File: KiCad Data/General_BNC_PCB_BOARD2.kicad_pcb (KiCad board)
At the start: 2 copper layers, 132.1 x 55.9 mm, 16 parts, among them P1 Potentiometer, Digikey P/N: 3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

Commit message: Add files via upload
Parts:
- added TP2: TestPoint, GENERAL PROJECT - NUMBER 1 LIBRARY - FOOTPRINTS:TestPoint, F.Cu at (71.1, 81.3)
- moved DP4T1 53.1 mm to (97.7, 101.6)
- moved SWT1 23.7 mm to (54.9, 106.5), turned to 90 degrees
- moved R1 23.4 mm to (66.0, 104.1)
- moved LED2 22.7 mm to (145.6, 103.6)
- moved LED3 22.7 mm to (151.1, 103.6)
- moved LED4 22.7 mm to (156.7, 103.6)
- moved LED1 22.7 mm to (140.1, 103.6)
- moved TP1 17.3 mm to (64.8, 81.3)
- moved P1 12.6 mm to (63.6, 83.2)
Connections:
- IDC1 pad 1: GND -> Net-(BNC1-Ext)
- IDC1 pad 10: Net-(BNC2-In) -> Net-(BNC3-In)
- IDC1 pad 11: Net-(BNC3-In) -> Net-(BNC4-In)
- IDC1 pad 12: Net-(BNC4-In) -> Net-(BNC5-In)
- IDC1 pad 13: Net-(BNC5-In) -> Net-(BNC6-In)
- IDC1 pad 14: Net-(BNC6-In) -> GND
- IDC1 pad 2: Net-(BNC1-Ext) -> Net-(BNC2-Ext)
- IDC1 pad 3: Net-(BNC2-Ext) -> Net-(BNC3-Ext)
- IDC1 pad 4: Net-(BNC3-Ext) -> Net-(BNC4-Ext)
- IDC1 pad 5: Net-(BNC4-Ext) -> Net-(BNC5-Ext)
- IDC1 pad 6: Net-(BNC5-Ext) -> Net-(BNC6-Ext)
- IDC1 pad 7: Net-(BNC6-Ext) -> GND
- IDC1 pad 8: GND -> Net-(BNC1-In)
- IDC1 pad 9: Net-(BNC1-In) -> Net-(BNC2-In)
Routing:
- net Net-(LED2-A): track 52.2 -> 85.2 mm
- net Net-(LED3-A): track 29.4 -> 62.1 mm
- net Net-(LED1-A): track 12.9 -> 44.9 mm
- net Net-(LED4-A): track 37.3 -> 68.8 mm
- net Net-(DP4T1-Pad1): track 64.3 -> 33.4 mm
- net Net-(P1-Pad3): track 32.0 -> 25.8 mm
- net Net-(BNC6-In): track 92.8 -> 97.6 mm
- net Net-(BNC5-In): track 119.5 -> 123.7 mm
- net Net-(BNC4-Ext): track 24.7 -> 27.3 mm
- net Net-(BNC1-In): track 61.0 -> 58.5 mm
- net Net-(BNC5-Ext): track 41.2 -> 42.7 mm
- net Net-(SWT1-B): track 12.8 -> 11.4 mm
- net Net-(BNC2-Ext): track 36.6 -> 35.4 mm
- net Net-(SWT1-A): track 23.0 -> 21.9 mm
- net Net-(BNC3-Ext): track 23.7 -> 22.6 mm
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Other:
- board size 132.1 x 55.9 mm -> 132.1 x 45.7 mm

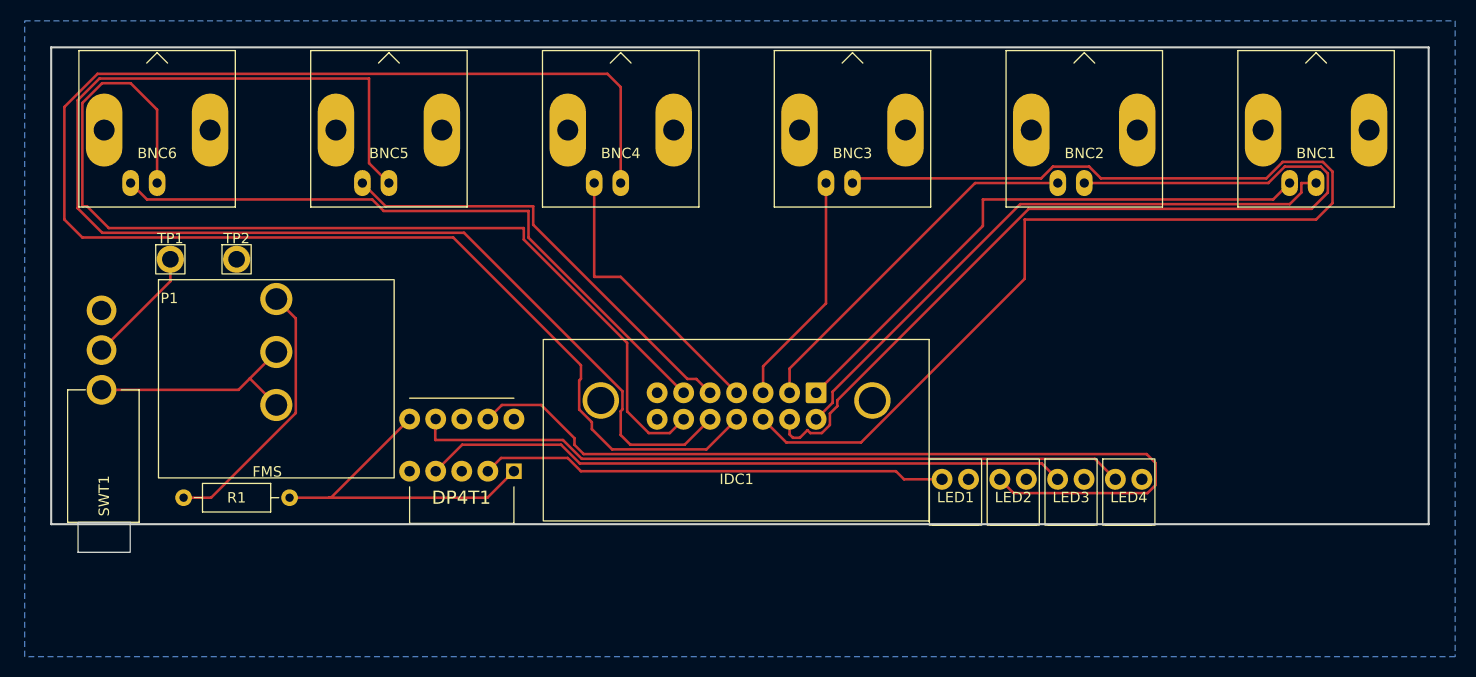
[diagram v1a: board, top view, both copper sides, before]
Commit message: Updated distance to edge of PCB for BNC's
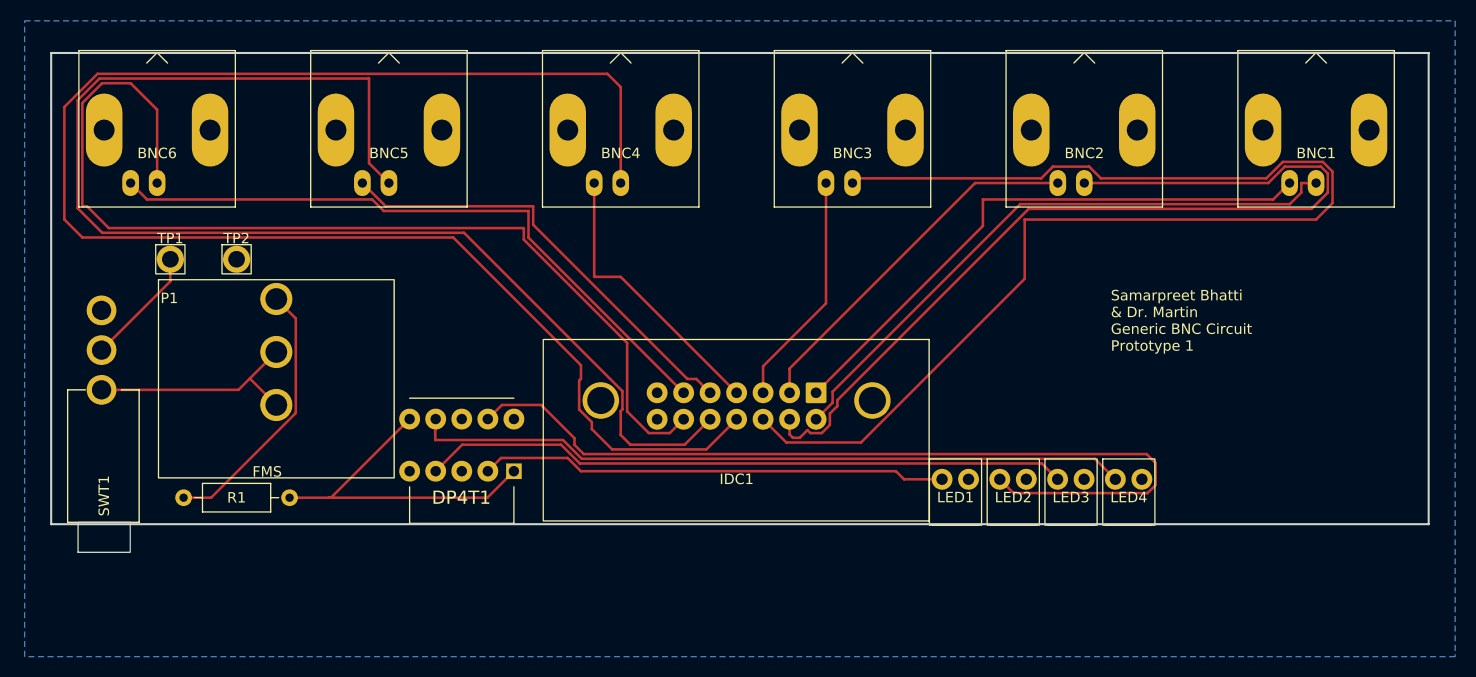
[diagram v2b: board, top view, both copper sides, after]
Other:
- board size 132.1 x 45.7 mm -> 132.1 x 45.2 mm
- board text added: "Samarpreet Bhatti & Dr. Martin Generic BNC Circuit Prototype 1"
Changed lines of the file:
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@@
     (pad "MH" thru_hole oval (at 5.08 -5.08) (size 3.5 7) (drill 2.01) (layers "*.Cu" "*.Mask"))
   )
-  (gr_rect (start 53.34 60.96) (end 185.42 106.68)
+  (gr_rect (start 53.34 61.5) (end 185.42 106.68)
     (stroke (width 0.2) (type default)) (fill none) (layer "Edge.Cuts"))
+  (gr_text "Samarpreet Bhatti\n& Dr. Martin\nGeneric BNC Circuit\nPrototype 1" (at 154.94 90.17) (layer "F.SilkS")
+    (effects (font (size 1 1) (thickness 0.15)) (justify left bottom))
+  )
   (segment (start 128.27 93.98) (end 128.27 95.0325) (width 0.25) (layer "F.Cu") (net 1))
   (segment (start 173.21 73.97) (end 173.21 74.88599) (width 0.25) (layer "F.Cu") (net 1))

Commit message: Updated board
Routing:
- net Net-(BNC6-Ext): track 62.8 -> 62.0 mm
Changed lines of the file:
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@@
   (segment (start 56.78 76.2) (end 58.87 78.29) (width 0.25) (layer "F.Cu") (net 11))
   (segment (start 84.123604 75.545) (end 62.535 75.545) (width 0.25) (layer "F.Cu") (net 12))
-  (segment (start 99.10901 79.20651) (end 99.10901 76.65) (width 0.25) (layer "F.Cu") (net 12))
-  (segment (start 99.10901 76.65) (end 85.228604 76.65) (width 0.25) (layer "F.Cu") (net 12))
-  (segment (start 85.228604 76.65) (end 84.123604 75.545) (width 0.25) (layer "F.Cu") (net 12))
+  (segment (start 99.10901 79.20651) (end 99.10901 78.103604) (width 0.25) (layer "F.Cu") (net 12))
+  (segment (start 98.845406 77.84) (end 86.418604 77.84) (width 0.25) (layer "F.Cu") (net 12))
+  (segment (start 62.535 75.545) (end 60.96 73.97) (width 0.25) (layer "F.Cu") (net 12))
+  (segment (start 86.418604 77.84) (end 84.123604 75.545) (width 0.25) (layer "F.Cu") (net 12))
+  (segment (start 99.10901 78.103604) (end 98.845406 77.84) (width 0.25) (layer "F.Cu") (net 12))
   (segment (start 113.9825 94.08) (end 99.10901 79.20651) (width 0.25) (layer "F.Cu") (net 12))
-  (segment (start 62.535 75.545) (end 60.96 73.97) (width 0.25) (layer "F.Cu") (net 12))
   (segment (start 76.795 96.022509) (end 76.795 86.955) (width 0.25) (layer "F.Cu") (net 13))
   (segment (start 76.795 86.955) (end 74.93 85.09) (width 0.25) (layer "F.Cu") (net 13))
